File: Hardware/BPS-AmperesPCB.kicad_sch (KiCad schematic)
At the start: 39 parts, among them IC1 INA241A5IDR, J1 Discharge V_In, J2 PeripheralCAN, J3 Charge V_In, J4 PeripheralCAN, J5 Conn_01x04, U1 INA145UA/2K5, U2 AMC1300BDWV

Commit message: small tweaks
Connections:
- net +3.3V: now also IC1.7 (REF1)
- net GND: now also IC1.3 (REF2)
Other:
- note added: "Filter"
- note added: "Ratiometric offset: 0V in = Vs/2 out"
- note added: "To-do: - verify datasheet values for bypass caps - values for scrutineering + jumper for mode selection - bidirectional current sense - low-pass filter - single ended signal into isolation after"
- note removed: "To-do: - verify datasheet values for bypass caps - values for scrutineering + jumper for mode selection - bidirectional current sense - singled ended signal into filter - move isolation after"
- moved on the sheet: IC1
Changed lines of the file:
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@@
 		)
 	)
+	(text "Filter"
+		(exclude_from_sim no)
+		(at 188.214 95.25 0)
+		(effects
+			(font
+				(size 1.27 1.27)
+			)
+		)
+	)
 	(text "Output Voltage Range: 0V - 0.25V"
 		(exclude_from_sim no)
@@
 	(text "Bidirectional current sense amp"
 		(exclude_from_sim no)
-		(at 125.222 94.234 0)
+		(at 126.492 94.234 0)
 		(effects
 			(font
@@
 		)
 	)
+	(text "Ratiometric offset: 0V in = Vs/2 out"
+		(exclude_from_sim no)
+		(at 123.952 123.444 0)
+		(effects
+			(font
+				(size 1.27 1.27)
+			)
+		)
+	)
 	(text "Current Sensor"
 		(exclude_from_sim no)
@@
 		)
 	)
-	(text "To-do:\n- verify datasheet values for bypass caps\n- values for scrutineering + jumper for mode selection\n- bidirectional current sense\n	- singled ended signal into filter\n	- move isolation after"
+	(text "To-do:\n- verify datasheet values for bypass caps\n- values for scrutineering + jumper for mode selection\n- bidirectional current sense\n	- low-pass filter\n	- single ended signal into isolation after"
 		(exclude_from_sim no)
 		(at 50.546 168.148 0)
@@
 	)
 	(junction
+		(at 105.41 109.22)
+		(diameter 0)
+		(color 0 0 0 0)
+	)
+	(junction
 		(at 62.23 106.68)
 		(diameter 0)
@@
 	)
 	(junction
+		(at 148.59 106.68)
+		(diameter 0)
+		(color 0 0 0 0)
+	)
+	(junction
 		(at 189.23 38.1)
 		(diameter 0)
@@
 	(wire
 		(pts
+			(xy 139.7 106.68) (xy 148.59 106.68)
+		)
+		(stroke
+			(width 0)
+			(type default)
+		)
+	)
+	(wire
+		(pts
 			(xy 76.2 44.45) (xy 106.68 44.45)
 		)
@@
 	(wire
 		(pts
+			(xy 139.7 109.22) (xy 148.59 109.22)
+		)
+		(stroke
+			(width 0)
+			(type default)
+		)
+	)
+	(wire
+		(pts
 			(xy 431.8 95.25) (xy 431.8 101.6)
 		)
@@
 	(wire
 		(pts
-			(xy 138.43 109.22) (xy 151.13 109.22)
-		)
-		(stroke
-			(width 0)
-			(type default)
-		)
-	)
-	(wire
-		(pts
 			(xy 161.29 60.96) (xy 171.45 60.96)
 		)
@@
 		)
 	)
+	(wire
+		(pts
+			(xy 148.59 106.68) (xy 148.59 101.6)
+		)
+		(stroke
+			(width 0)
+			(type default)
+		)
+	)
 	(polyline
 		(pts
@@
 	(wire
 		(pts
-			(xy 138.43 104.14) (xy 144.78 104.14)
+			(xy 139.7 104.14) (xy 146.05 104.14)
 		)
 		(stroke
@@
 	(wire
 		(pts
-			(xy 102.87 106.68) (xy 102.87 113.03)
+			(xy 339.09 151.13) (xy 359.41 151.13)
 		)
 		(stroke
@@
 	(wire
 		(pts
-			(xy 339.09 151.13) (xy 359.41 151.13)
+			(xy 171.45 29.21) (xy 161.29 29.21)
 		)
 		(stroke
@@
 	(wire
 		(pts
-			(xy 171.45 29.21) (xy 161.29 29.21)
+			(xy 359.41 171.45) (xy 359.41 167.64)
 		)
 		(stroke
@@
 	(wire
 		(pts
-			(xy 359.41 171.45) (xy 359.41 167.64)
+			(xy 171.45 53.34) (xy 161.29 53.34)
 		)
 		(stroke
@@
 	(wire
 		(pts
-			(xy 171.45 53.34) (xy 161.29 53.34)
+			(xy 105.41 106.68) (xy 111.76 106.68)
 		)
 		(stroke
@@
 		)
 	)
-	(wire
-		(pts
-			(xy 151.13 109.22) (xy 151.13 101.6)
-		)
-		(stroke
-			(width 0)
-			(type default)
-		)
-	)
 	(polyline
 		(pts
@@
 	(wire
 		(pts
-			(xy 110.49 106.68) (xy 102.87 106.68)
+			(xy 105.41 106.68) (xy 105.41 109.22)
 		)
 		(stroke
@@
 	(wire
 		(pts
-			(xy 138.43 111.76) (xy 144.78 111.76)
+			(xy 139.7 111.76) (xy 146.05 111.76)
 		)
 		(stroke
@@
 	(wire
 		(pts
-			(xy 105.41 104.14) (xy 110.49 104.14)
+			(xy 106.68 104.14) (xy 111.76 104.14)
+		)
+		(stroke
+			(width 0)
+			(type default)
+		)
+	)
+	(wire
+		(pts
+			(xy 148.59 109.22) (xy 148.59 106.68)
+		)
+		(stroke
+			(width 0)
+			(type default)
+		)
+	)
+	(wire
+		(pts
+			(xy 105.41 109.22) (xy 105.41 113.03)
 		)
 		(stroke
@@
 		)
 	)
+	(wire
+		(pts
+			(xy 105.41 109.22) (xy 111.76 109.22)
+		)
+		(stroke
+			(width 0)
+			(type default)
+		)
+	)
 	(polyline
 		(pts
@@
 	)
 	(label "IN-"
-		(at 105.41 104.14 0)
+		(at 106.68 104.14 0)
 		(effects
 			(font
@@
 	)
 	(label "i_out"
-		(at 144.78 111.76 180)
+		(at 146.05 111.76 180)
 		(effects
 			(font
@@
 	)
 	(label "IN+"
-		(at 144.78 104.14 180)
+		(at 146.05 104.14 180)
 		(effects
 			(font
@@
 	(symbol
 		(lib_id "power:+3.3V")
-		(at 151.13 101.6 0)
+		(at 148.59 101.6 0)
 		(unit 1)
 		(exclude_from_sim no)
@@
 		(fields_autoplaced yes)
 		(property "Reference" "#PWR071"
-			(at 151.13 105.41 0)
+			(at 148.59 105.41 0)
 			(effects
 				(font
@@
 		)
 		(property "Value" "+3.3V"
-			(at 151.13 96.52 0)
+			(at 148.59 96.52 0)
 			(effects
 				(font
@@
 		)
 		(property "Footprint" ""
-			(at 151.13 101.6 0)
+			(at 148.59 101.6 0)
 			(effects
 				(font
@@
 		)
 		(property "Datasheet" ""
-			(at 151.13 101.6 0)
+			(at 148.59 101.6 0)
 			(effects
 				(font
@@
 		)
 		(property "Description" "Power symbol creates a global label with name \"+3.3V\""
-			(at 151.13 101.6 0)
+			(at 148.59 101.6 0)
 			(effects
 				(font
@@
 	(symbol
 		(lib_id "INA241:INA241A5IDR")
-		(at 110.49 104.14 0)
+		(at 111.76 104.14 0)
 		(unit 1)
 		(exclude_from_sim no)
@@
 		(fields_autoplaced yes)
 		(property "Reference" "IC1"
-			(at 124.46 96.52 0)
+			(at 125.73 96.52 0)
 			(effects
 				(font
@@
 		)
 		(property "Value" "INA241A5IDR"
-			(at 124.46 99.06 0)
+			(at 125.73 99.06 0)
 			(effects
 				(font
@@
 		)
 		(property "Footprint" "SOIC127P600X175-8N"
-			(at 134.62 199.06 0)
+			(at 135.89 199.06 0)
 			(effects
 				(font
@@
 		)
 		(property "Datasheet" "https://www.ti.com/lit/ds/symlink/ina241a.pdf?ts=1712302873194&ref_url=https%253A%252F%252Fwww.mouser.in%252F"
-			(at 134.62 299.06 0)
+			(at 135.89 299.06 0)
 			(effects
 				(font
@@
 		)
 		(property "Description" "Current Sense Amplifiers -5-V to 110-V bidirectional ultraprecise current sense amplifier with enhanced PWM rejection 8-SOIC -40 to 125"
-			(at 110.49 104.14 0)
+			(at 111.76 104.14 0)
 			(effects
 				(font
@@
 		)
 		(property "Height" "1.75"
-			(at 134.62 499.06 0)
+			(at 135.89 499.06 0)
 			(effects
 				(font
@@
 		)
 		(property "Mouser Part Number" "595-INA241A5IDR"
-			(at 134.62 599.06 0)
+			(at 135.89 599.06 0)
 			(effects
 				(font
@@
 		)
 		(property "Mouser Price/Stock" "https://www.mouser.co.uk/ProductDetail/Texas-Instruments/INA241A5IDR?qs=ST9lo4GX8V3geNjZJSmQBQ%3D%3D"
-			(at 134.62 699.06 0)
+			(at 135.89 699.06 0)
 			(effects
 				(font
@@
 		)
 		(property "Manufacturer_Name" "Texas Instruments"
-			(at 134.62 799.06 0)
+			(at 135.89 799.06 0)
 			(effects
 				(font
@@
 		)
 		(property "Manufacturer_Part_Number" "INA241A5IDR"
-			(at 134.62 899.06 0)
+			(at 135.89 899.06 0)
 			(effects
 				(font
@@
 	(symbol
 		(lib_id "power:GND")
-		(at 102.87 113.03 0)
+		(at 105.41 113.03 0)
 		(unit 1)
 		(exclude_from_sim no)
@@
 		(fields_autoplaced yes)
 		(property "Reference" "#PWR070"
-			(at 102.87 119.38 0)
+			(at 105.41 119.38 0)
 			(effects
 				(font
@@
 		)
 		(property "Value" "GND"
-			(at 102.87 118.11 0)
+			(at 105.41 118.11 0)
 			(effects
 				(font
@@
 		)
 		(property "Footprint" ""
-			(at 102.87 113.03 0)
+			(at 105.41 113.03 0)
 			(effects
 				(font
@@
 		)
 		(property "Datasheet" ""
-			(at 102.87 113.03 0)
+			(at 105.41 113.03 0)
 			(effects
 				(font
@@
 		)
 		(property "Description" "Power symbol creates a global label with name \"GND\" , ground"
-			(at 102.87 113.03 0)
+			(at 105.41 113.03 0)
 			(effects
 				(font
@@
 			)
 		)
-		(pin "CAN_HIGH" input
+		(pin "CAN_HIGH" bidirectional
 			(at 129.54 41.91 0)
 			(effects
@@
 			)
 		)
-		(pin "CAN_LOW" input
+		(pin "CAN_LOW" bidirectional
 			(at 129.54 44.45 0)
 			(effects
@@
 			)
 		)
-		(pin "CAN_RX" output
+		(pin "CAN_RX" bidirectional
 			(at 106.68 41.91 180)
 			(effects
@@
 			)
 		)
-		(pin "CAN_TX" input
+		(pin "CAN_TX" bidirectional
 			(at 106.68 44.45 180)
 			(effects

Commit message: shunt to current sense to isolation done?? need to select values
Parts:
- removed C5, C6: 1uF, Capacitor_SMD:C_0805_2012Metric, symbol Device:C
- removed INN1, INP1, OUTN1, OUTP1: TestPoint, TestPoint:TestPoint_Keystone_5005-5009_Compact, symbol Connector:TestPoint
- added C27, C28: 1uF, symbol Device:C_Small
- added R22, R23: ??, symbol Device:R_Small
- added TP11: SHUNT-, symbol Connector:TestPoint
- added TP12: SHUNT+, symbol Connector:TestPoint
- added TP13: OUT+, symbol Connector:TestPoint
- added TP14: OUT-, symbol Connector:TestPoint
- C3, R4, R6: now not fitted
- J5: value Conn_01x04 -> Shunt Conn
- U2: now fitted
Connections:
- net +3V3 HV is gone; now on net +3.3V HV: J5.4 (Pin_4)
- net +3.3V: now also C28.1; no longer IC1.6 (VS), IC1.7 (REF1)
- net +3.3V HV: now also IC1.6 (VS), C27.2, R22.1
- net GND: now also C28.2; no longer IC1.2 (GND), IC1.3 (REF2)
- net GND HV: now also IC1.2 (GND), C27.1, R23.2; no longer J5.2 (Pin_2), R6.2
- net OUTN: no longer U2.6 (-)
- net OUTP: no longer U2.7 (+)
- net at R4.2: no longer J5.1 (Pin_1)
- net IN+: no longer names the net of C3.1, R4.1
- net IN+: no longer IC1.8 (IN+), U2.2 (+)
- net IN-: no longer names the net of C3.2, R6.1
- net IN-: no longer IC1.1 (IN-), U2.3 (-)
- net i_out renamed SENSE+
- net SENSE+: now also U2.2 (+)
- new net OUT+: TP13.1, U2.7 (+)
- new net OUT-: TP14.1, U2.6 (-)
- new net SENSE-: IC1.3 (REF2), IC1.7 (REF1), R22.2, R23.1, U2.3 (-)
- new net SHUNT+: IC1.8 (IN+), J5.1 (Pin_1), TP12.1
- new net SHUNT-: IC1.1 (IN-), J5.2 (Pin_2), TP11.1
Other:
- note added: "Current Range: (-) Charge: 32A thru Elcon; max 54A from cell (+) Discharge: 70A"
- note added: "Divider: V = Vin * [R2 / (R1 + R2)]"
- note added: "Expected current range: -32A to +70A"
- note added: "Gain: Max current: Max voltage:"
- note added: "Input Voltage Range: +- 0.25 V"
- note added: "Isolation"
- note added: "Output Voltage Range:"
- note added: "Reference voltage: Total current range ~105A With ref voltage (32A / 105A) * 3.3V = 1V, * 0A = 1V * 70A = 3.3V * -32A = 0V"
- note added: "Shunt -> current sense -> isolation -> filter"
- note added: "To-do: - verify datasheet values for bypass caps - values for scrutineering + jumper for mode selection - bidirectional current sense: bias for discharge (70A) - single ended signal into isolation - any amplification needed - filter"
- note removed: "- Max current range:"
- note removed: "Expected Range for Current: 0A - 120A"
- note removed: "Filter"
- note removed: "Input Voltage Range: 0V - 0.03V"
- note removed: "Output Voltage Range: 0V - 0.25V"
- note removed: "Ratiometric offset: 0V in = Vs/2 out"
- note removed: "To-do: - verify datasheet values for bypass caps - values for scrutineering + jumper for mode selection - bidirectional current sense - low-pass filter - single ended signal into isolation after"
- moved on the sheet: IC1, J5

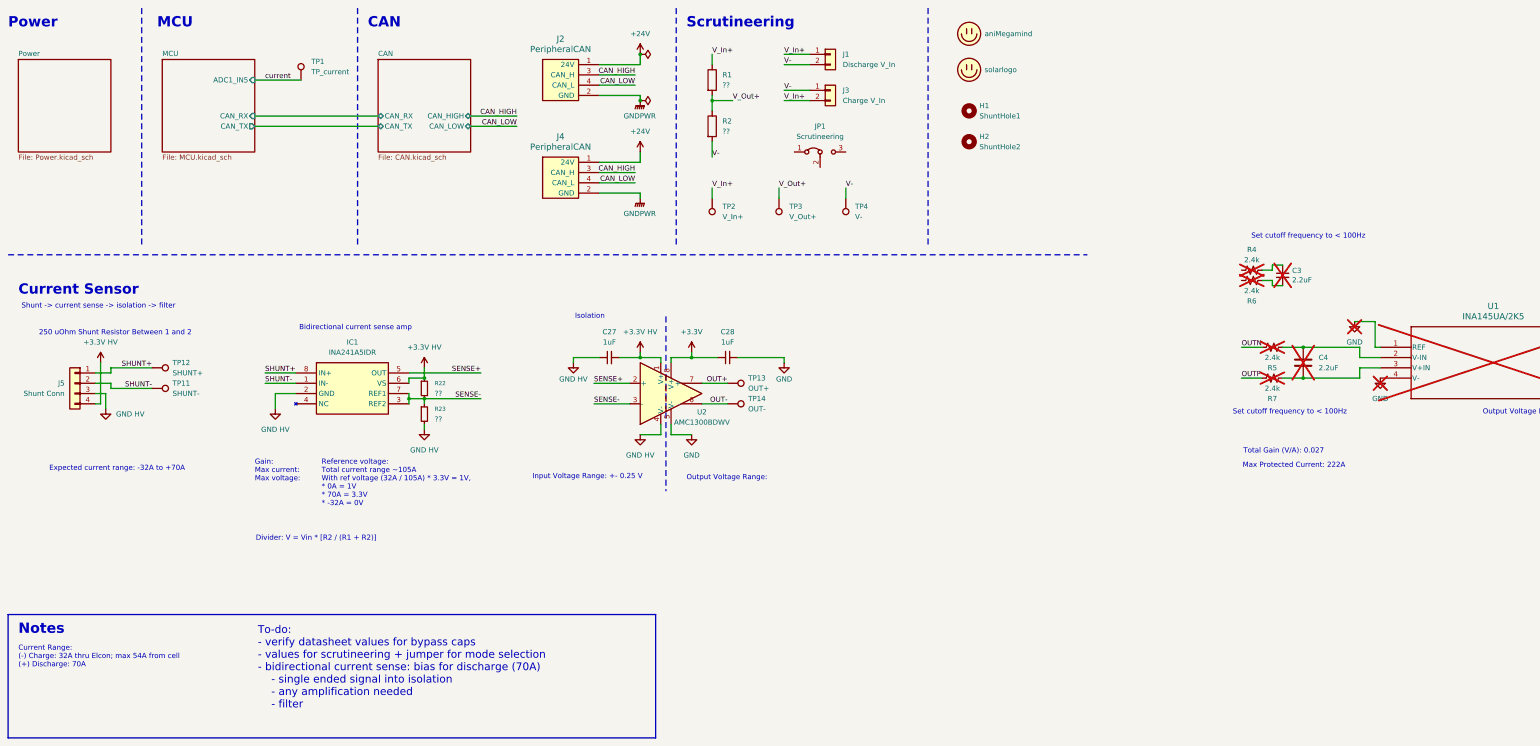
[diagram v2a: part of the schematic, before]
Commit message: new isolated amp, filter stage; need to select values
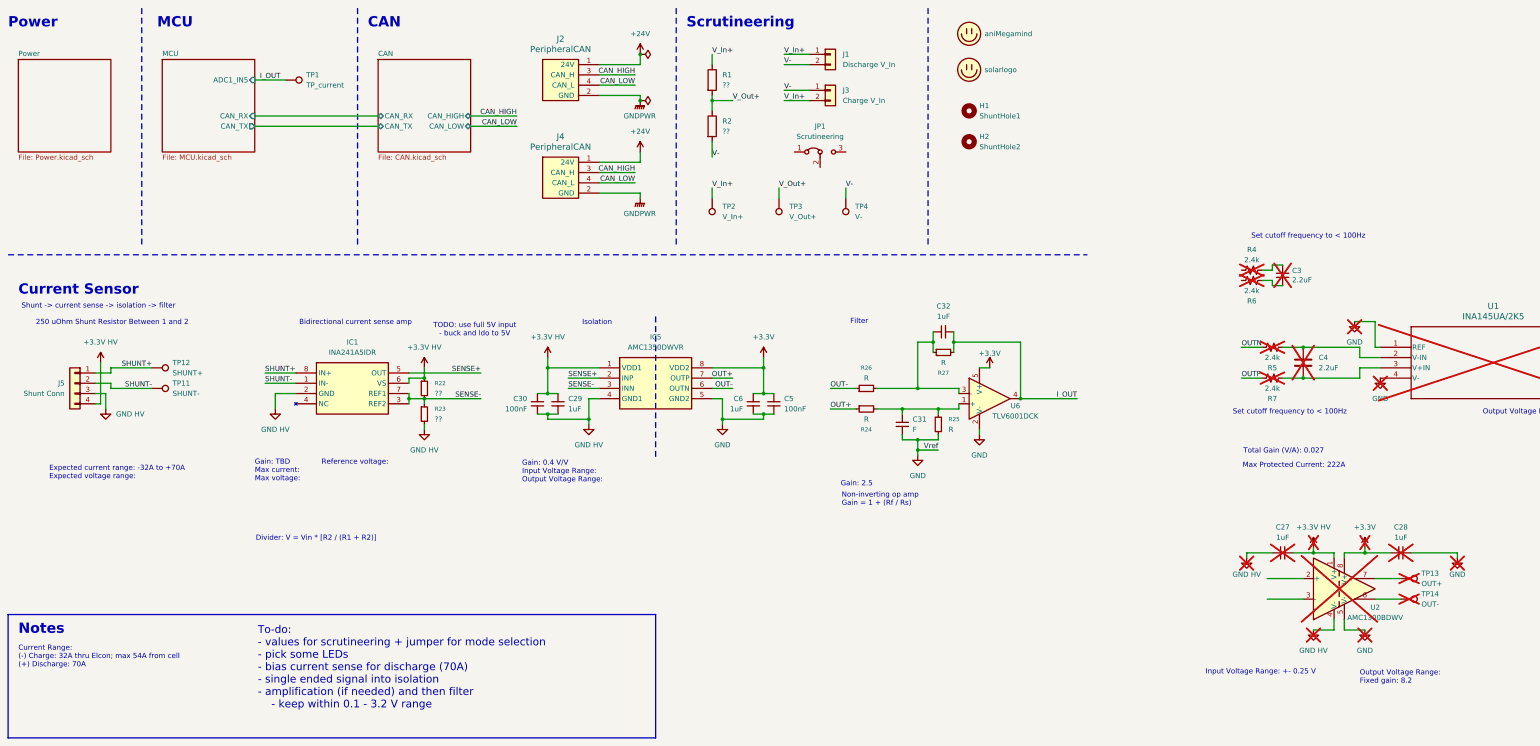
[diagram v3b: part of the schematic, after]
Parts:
- added C29, C32, C6: 1uF, symbol Device:C_Small
- added C30, C5: 100nF, symbol Device:C_Small
- added C31: F, symbol Device:C_Small
- added IC5: AMC1350DWVR, SOIC127P1150X280-8N, symbol AMC1350:AMC1350DWVR
- added R24, R25, R26, R27: R, symbol Device:R_Small
- added U6: TLV6001DCK, Package_TO_SOT_SMD:SOT-353_SC-70-5, symbol Amplifier_Operational:TLV6001DCK
- C27, C28, TP13, TP14, U2: now not fitted
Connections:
- net +3.3V: now also C5.1, C6.1, IC5.8 (VDD2), U6.5 (V+)
- net +3.3V HV: now also C29.1, C30.1, IC5.1 (VDD1)
- net GND: now also C31.2, C5.2, C6.2, IC5.5 (GND2), R25.1, U6.2 (V-)
- net GND HV: now also C29.2, C30.2, IC5.4 (GND1)
- net OUT+: now also IC5.7 (OUTP), R24.1; no longer TP13.1, U2.7 (+)
- net OUT-: now also IC5.6 (OUTN), R26.1; no longer TP14.1, U2.6 (-)
- net SENSE+: now also IC5.2 (INP); no longer U2.2 (+)
- net SENSE-: now also IC5.3 (INN); no longer U2.3 (-)
- net current: no longer TP1.1
- new net: C31.1, R24.2, R25.2, U6.1 (+)
- new net: TP14.1, U2.6 (-)
- new net: TP13.1, U2.7 (+)
- new net: C32.1, R26.2, R27.1, U6.3 (-)
- new net I_OUT: C32.2, R27.2, TP1.1, U6.4
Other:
- note added: "Expected current range: -32A to +70A Expected voltage range:"
- note added: "Filter"
- note added: "Gain: 0.4 V/V Input Voltage Range: Output Voltage Range:"
- note added: "Gain: 2.5"
- note added: "Gain: TBD Max current: Max voltage:"
- note added: "Non-inverting op amp Gain = 1 + (Rf / Rs)"
- note added: "Output Voltage Range: Fixed gain: 8.2"
- note added: "Reference voltage:"
- note added: "TODO: use full 5V input - buck and ldo to 5V"
- note added: "To-do: - values for scrutineering + jumper for mode selection - pick some LEDs - bias current sense for discharge (70A) - single ended signal into isolation - amplification (if needed) and then filter - keep within 0.1 - 3.2 V range"
- note removed: "Expected current range: -32A to +70A"
- note removed: "Gain: Max current: Max voltage:"
- note removed: "Output Voltage Range:"
- note removed: "Reference voltage: Total current range ~105A With ref voltage (32A / 105A) * 3.3V = 1V, * 0A = 1V * 70A = 3.3V * -32A = 0V"
- note removed: "To-do: - verify datasheet values for bypass caps - values for scrutineering + jumper for mode selection - bidirectional current sense: bias for discharge (70A) - single ended signal into isolation - any amplification needed - filter"
- moved on the sheet: TP1

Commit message: lowk got some filter values from chat PLEASE PLEASE PLEASE VERIFY LATER
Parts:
- added C35: 1nF, symbol Device:C_Small
- C31: value F -> 330pF
- C32: value 1uF -> 330pF
- R24, R26: value R -> 20K
- R25, R27: value R -> 50K
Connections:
- net GND: no longer C31.2, R25.1
- net SENSE+: now also C35.1
- net SENSE-: now also C31.2, R25.1, C35.2
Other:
- note added: "Difference amp Vout = (R2/R1) * (Vp - Vn)"
- note added: "Gain: 2.5 With all resistors equal, Vout = 2.5(VoutP - VoutN) + Vref"
- note added: "Place caps as close to the IC as possible"
- note removed: "Gain: 2.5"
- note removed: "Non-inverting op amp Gain = 1 + (Rf / Rs)"
- moved on the sheet: C29, C30, C31, C32, C5, C6, IC1, J5, R22, R23, R25, R27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

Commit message: plz review
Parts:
- C31, C32: value 330pF -> ??
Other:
- note added: "(TBD) Shunt Resistor Between 1 and 2 - old value was 250 uOhm"
- note added: "Current Range: Charge (-): 32A thru Elcon; max 54A from cell Discharge (+): 70A Voltage Range: 32 cells, 2.6 - 4.1 V range => 83.2V to 131.2V"
- note added: "Expected current range: -32A to +70A Expected voltage range: aprox. 83.2 to 131.2 (V)"
- note added: "Gain: 0.4 V/V Input Voltage Range: 0 - 3.3 V Output Voltage Range: 0 - 1.32 V"
- note added: "Gain: 2.5 V/V (??) Vout = 2.5(VoutP - VoutN) + Vref Cutoff freq: figure out"
- note added: "Gain: TBD Max input voltage: -5 to 110V Max current:"
- note added: "Low-Pass Filter"
- note added: "Reference voltage: 1.04 V - bias for discharge (70A) out of total 102A range - (32A / 102A) * 3.3V = 1.04 V"
- note added: "To-do: - values for everything - scrutineering - pick some LEDs - bias current sense for discharge (70A) - single ended signal into isolation - amplification (if needed) and then filter - keep within 0.1 - 3.2 V range"
- note removed: "250 uOhm Shunt Resistor Between 1 and 2"
- note removed: "Current Range: (-) Charge: 32A thru Elcon; max 54A from cell (+) Discharge: 70A"
- note removed: "Expected current range: -32A to +70A Expected voltage range:"
- note removed: "Filter"
- note removed: "Gain: 0.4 V/V Input Voltage Range: Output Voltage Range:"
- note removed: "Gain: 2.5 With all resistors equal, Vout = 2.5(VoutP - VoutN) + Vref"
- note removed: "Gain: TBD Max current: Max voltage:"
- note removed: "Place caps as close to the IC as possible"
- note removed: "Reference voltage:"
- note removed: "To-do: - values for scrutineering + jumper for mode selection - pick some LEDs - bias current sense for discharge (70A) - single ended signal into isolation - amplification (if needed) and then filter - keep within 0.1 - 3.2 V range"
- moved on the sheet: C29, C30, C31, C32, C35, C5, C6, IC1, IC5, J5, R22, R23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
